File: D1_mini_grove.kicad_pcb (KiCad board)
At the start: 2 copper layers, 25.7 x 34.3 mm, 9 parts, among them P1 Connector_Generic:Conn_01x08, P2 Connector_Generic:Conn_01x08

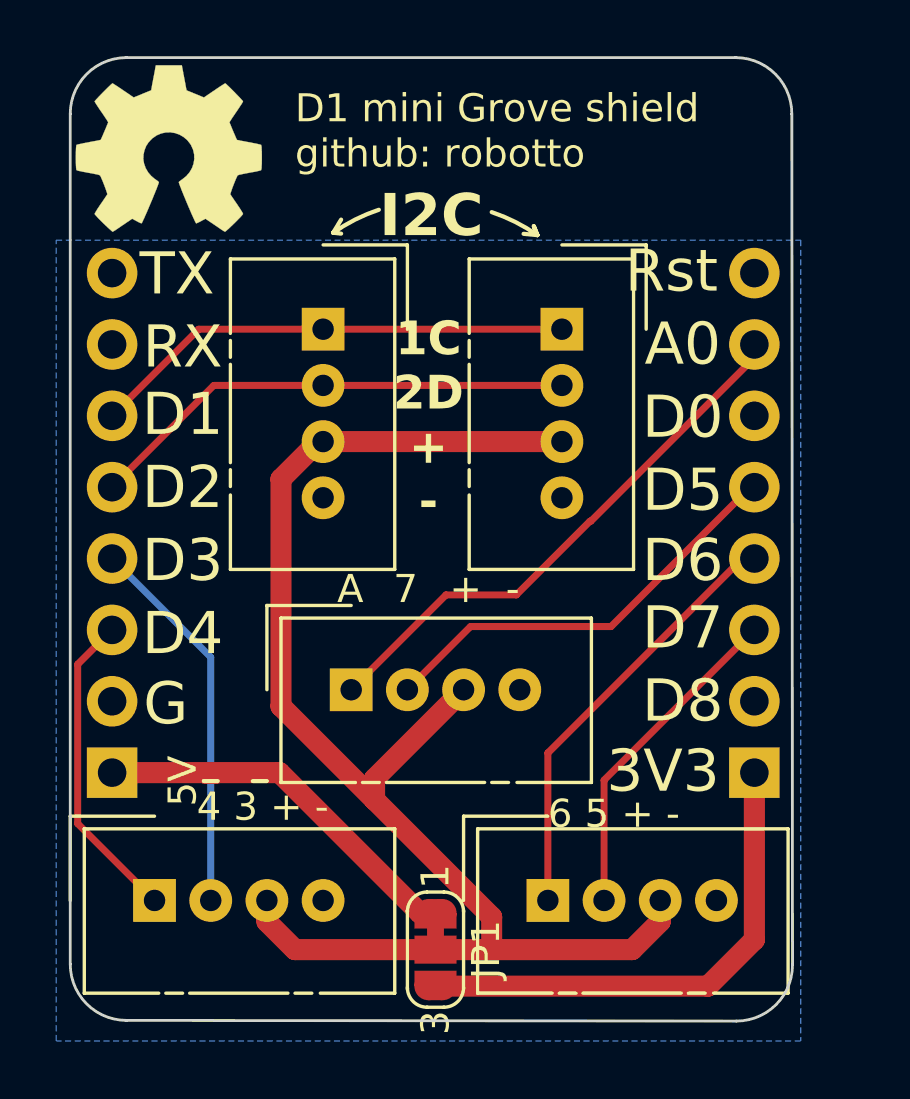
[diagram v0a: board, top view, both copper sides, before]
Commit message: Topsilk rearranged, shoud fix #1
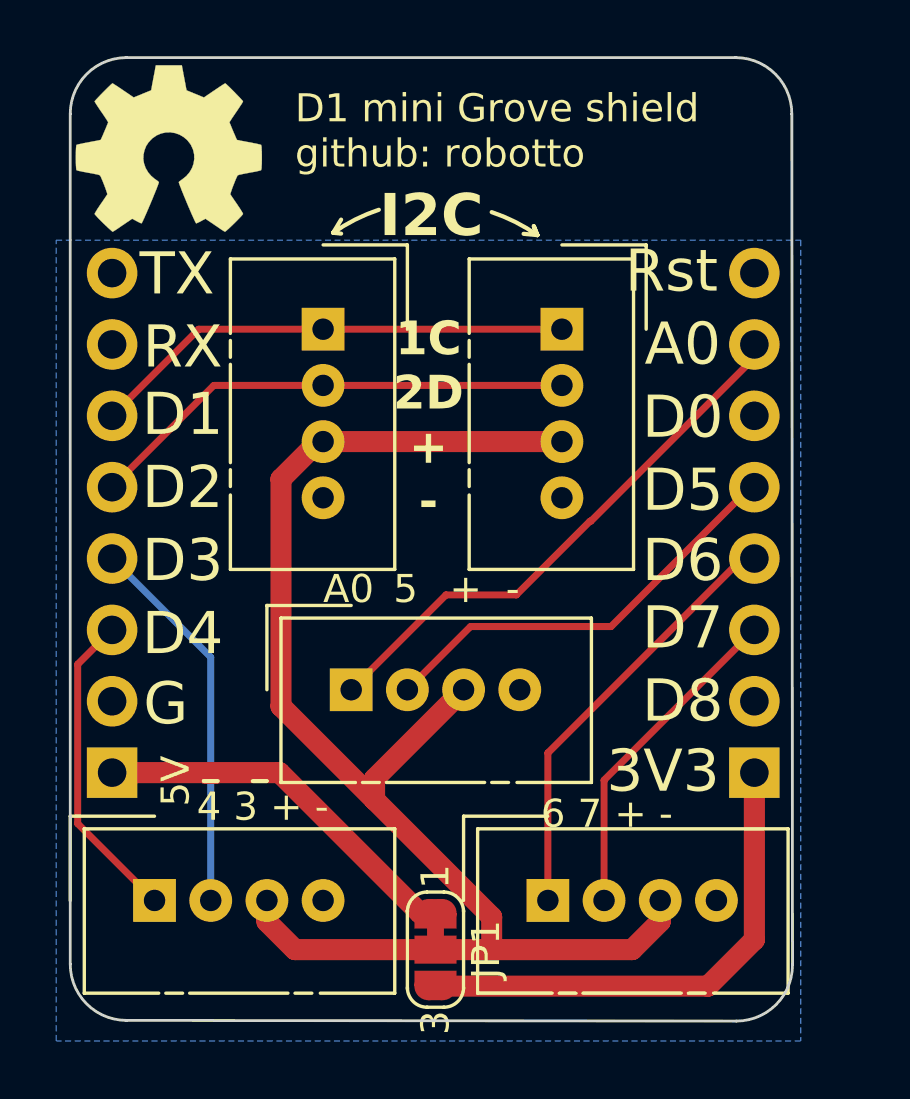
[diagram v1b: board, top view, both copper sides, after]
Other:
- board text added: "5"
- board text added: "6 7 + -"
- board text removed: "6 5 + -"
- board text removed: "7"
- board text removed: "A"
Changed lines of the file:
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@@
 		)
 	)
-	(gr_text "A"
-		(at 135.5 98 0)
+	(gr_text "A0"
+		(at 135 98 0)
 		(layer "F.SilkS")
 		(effects
@@
 		)
 	)
-	(gr_text "7"
+	(gr_text "5"
 		(at 137.5 98 0)
 		(layer "F.SilkS")
@@
 		)
 	)
-	(gr_text "6 5 + -"
-		(at 143 106 0)
+	(gr_text "6 7 + -"
+		(at 142.75 106 0)
 		(layer "F.SilkS")
 		(effects
@@
 	)
 	(gr_text "5V"
-		(at 130 104.25 90)
+		(at 129.75 104.25 90)
 		(layer "F.SilkS")
 		(effects

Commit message: flipped some stuff around
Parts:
- 1_2_IIC1, 1_2_IIC2, 3_4, 5_6, A0_7, REF**: moved to B.Cu
- P1, P2: moved to F.Cu
- moved REF** 18.4 mm to (147.9, 81.8), turned to 180 degrees
- turned 1_2_IIC1 to 180 degrees
- turned 1_2_IIC2 to 180 degrees
- turned 3_4 to -90 degrees
- turned 5_6 to -90 degrees
- turned A0_7 to -90 degrees
- turned P1 to 180 degrees
- turned P2 to 180 degrees
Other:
- board text added: "- + 3 4"
- board text added: "- + 7 6"
- board text removed: "4 3 + -"
- board text removed: "6 7 + -"

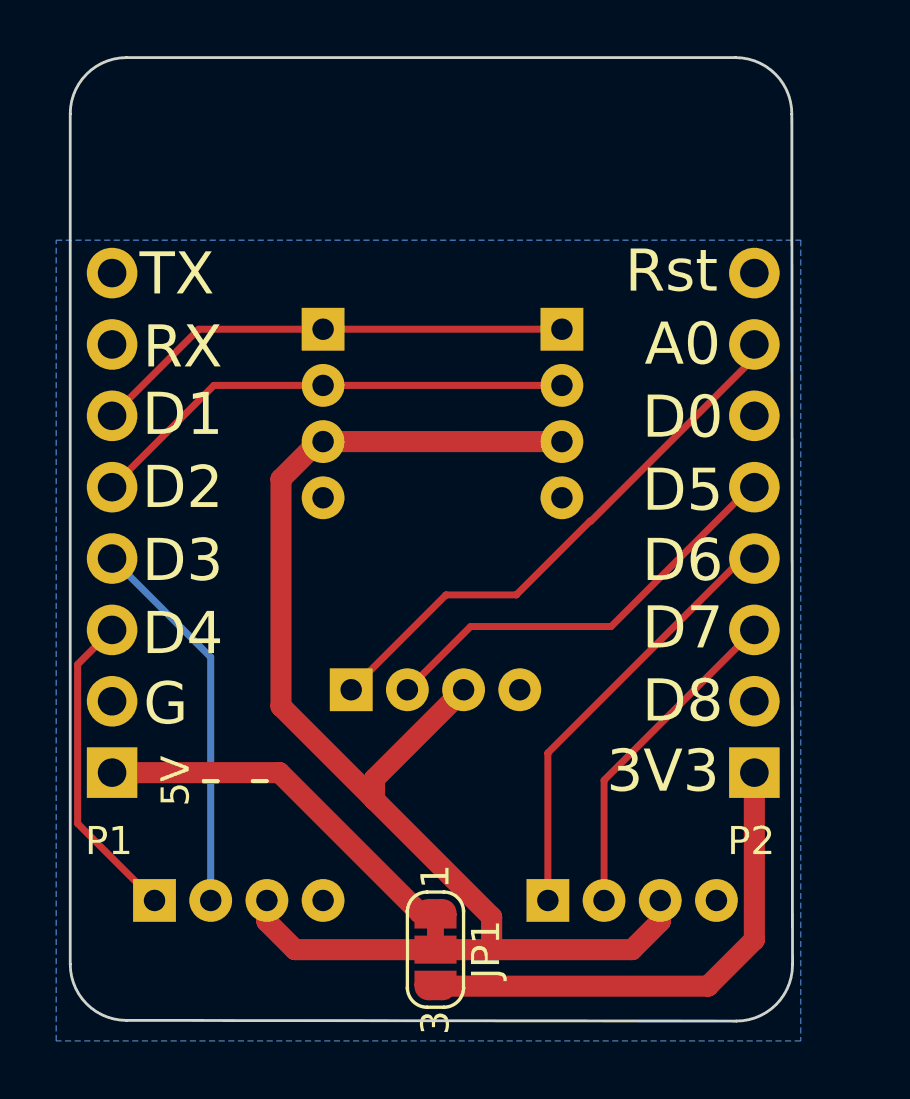
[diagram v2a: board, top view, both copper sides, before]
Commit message: Finetuned some layout
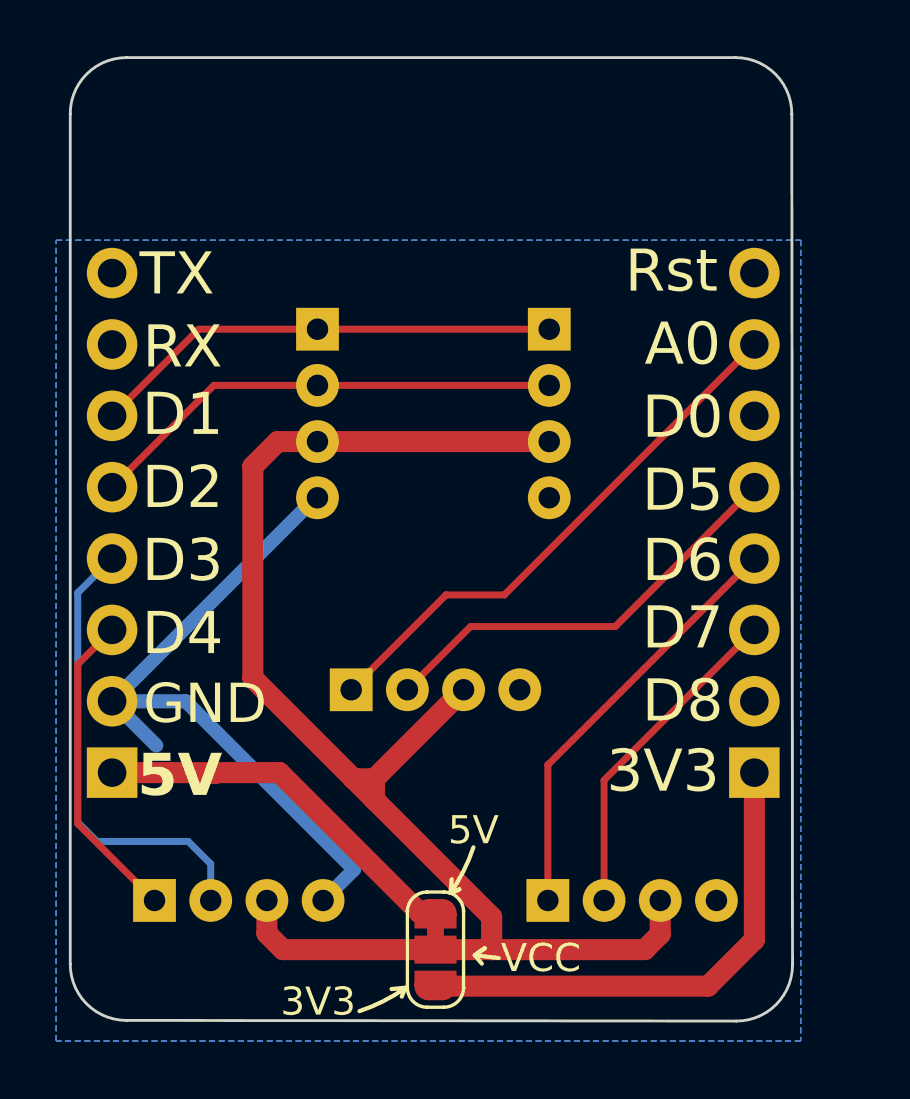
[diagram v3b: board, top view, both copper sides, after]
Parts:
- moved 1_2_IIC2 0.45 mm to (143.1, 88.2)
- moved 1_2_IIC1 0.20 mm to (134.8, 88.2)
- renumbered JP1 to VCC
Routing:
- net GND: track 0.10 -> 25.2 mm
- net /D3: track 13.6 -> 16.7 mm
- net VCC: track 52.0 -> 54.5 mm
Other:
- board text added: "(tx)"
- board text added: "1C"
- board text added: "2D"
- board text added: "GND"
- board text added: "KEEP HIGH AT BOOT!"
- board text removed: "1C 2D + -"
- board text removed: "G"
